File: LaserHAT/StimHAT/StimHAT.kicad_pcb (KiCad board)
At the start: 4 copper layers, 65 x 64.5 mm, 112 parts, among them J1 GPIO, J10 OLED 0.91 (GND VCC SCL SDA), J101 ELECTRODE E1/E2, J102 B4B-PH-K-S(LF)(SN), J103 5V TO DC-DC POD, J5 GT-USB-7010ASV, J6 BNC TRIGGER IN, J7 BNC STIM OUT, Q3 AP30P30Q, Q4 DMMT5401, Q5 AP30P30Q, SW10 MSK12C02, SW6 TS-1088-AR02016, SW7 SKRHADE010, SW9 TS-1088-AR02016, U1 M24C32-WDW6TP, U101 ISO7741FDBQR, U104 TLV76050DBZR, U105 DAC60501ZDGSR, U106 OPA2192IDGKR, U107 CD74HC4053PWR, U108 DG418DY-T1-E3, U109 ISO1640BDR, U110 TLV1702AIDGKR, U4 MCP1700T-3302E/MB, U5 AP2171W, U6 CH340N, U7 MSPM0G1507SRHBR, U8 74LVC2G17GW

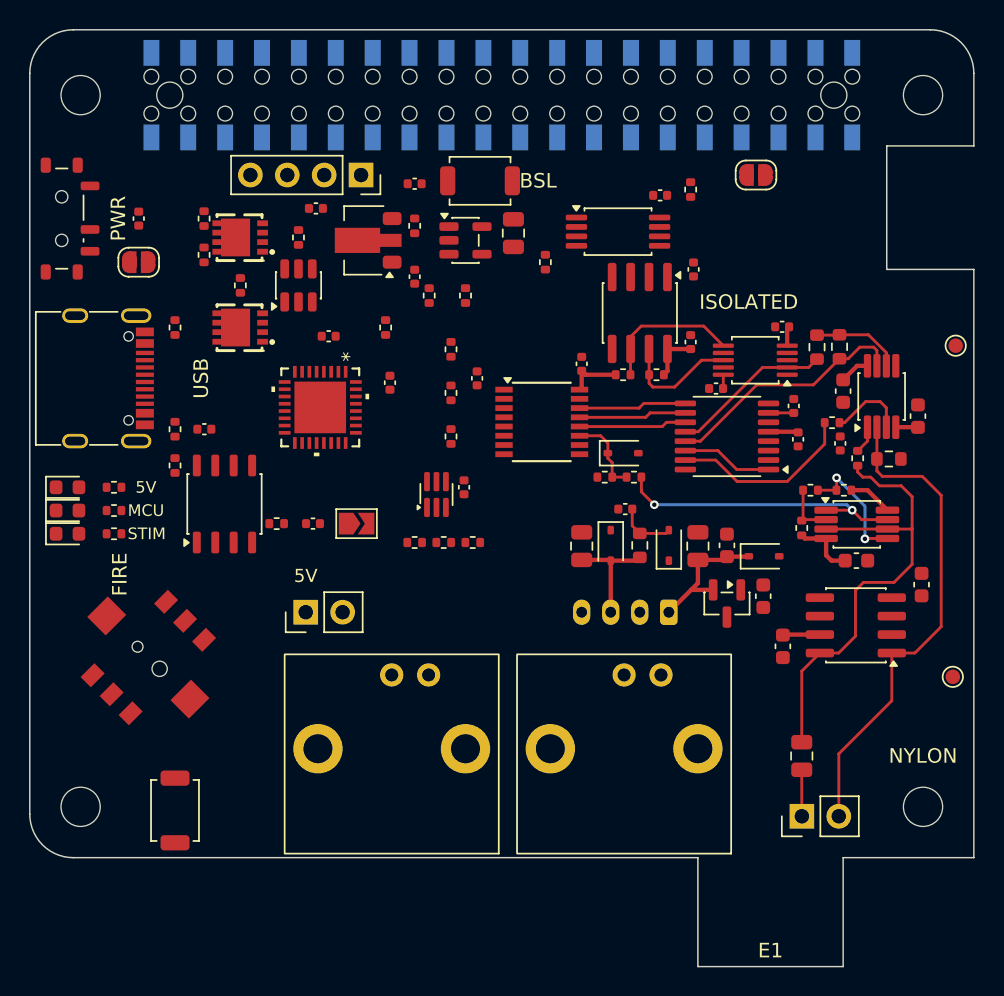
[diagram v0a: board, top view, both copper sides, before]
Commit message: StimHAT: regions/strips/planes reshaped to the user's placement, tab removed, F/B ground pours + In2 power islands, isolated-block power routed (vias to the islands, maze for the negative rails, stitching vias); DRC 0 errors, 123 HAT-side opens
Co-Authored-By: Claude Fable 5.1 <noreply@anthropic.com>
Claude-Session: https://claude.ai/code/session_015kiXLxnPpBaXdXJu2EMvn7
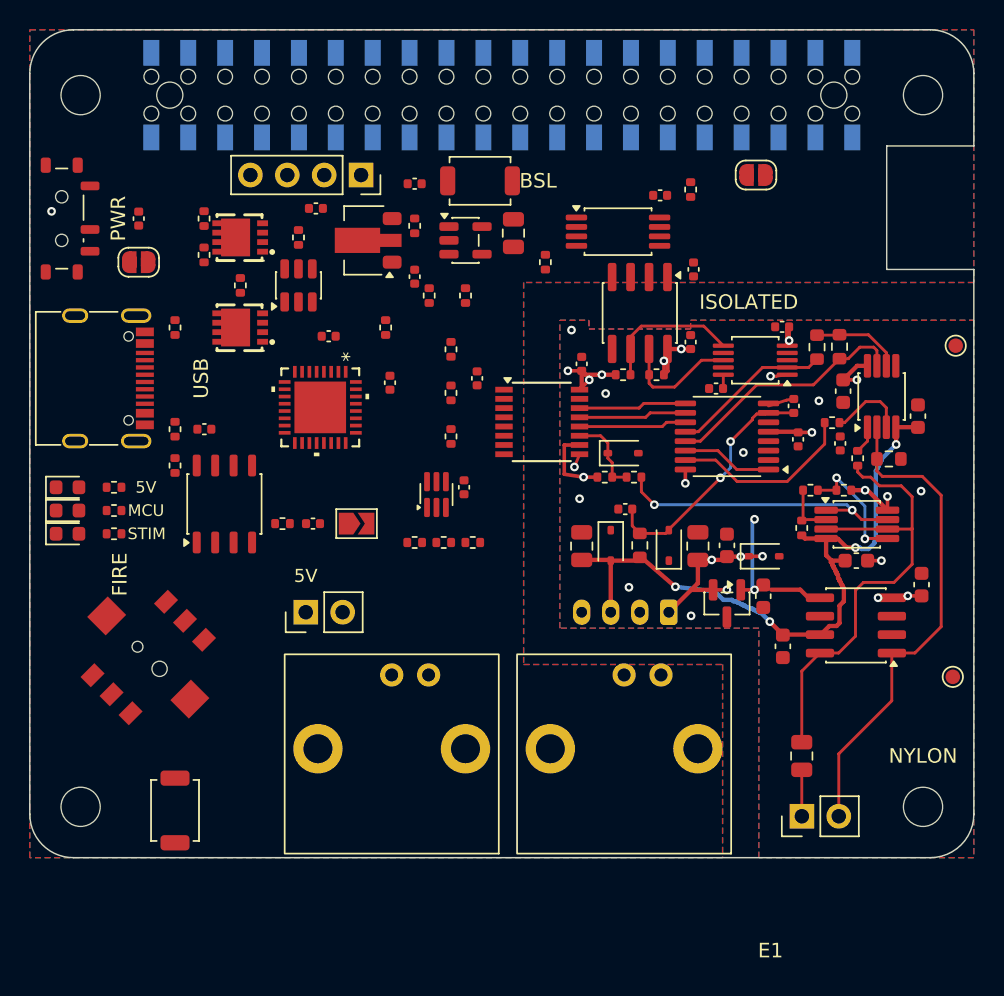
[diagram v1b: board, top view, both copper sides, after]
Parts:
- moved R3 0.40 mm to (17.4, 34.0)
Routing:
- net -V_STIM: track 16.1 -> 46.9 mm, vias 0 -> 4
- net +5V_ISO: track 10.7 -> 34.3 mm, vias 0 -> 12
- net -5V_ISO: track 5.72 -> 17.1 mm, vias 0 -> 2
- net +V_STIM: track 14.7 -> 24.2 mm, vias 0 -> 10
- net GND_ISO: track 0.00 -> 2.74 mm, vias 0 -> 9
- net GND: vias 0 -> 1
- added copper zone on In2.Cu, net +5V
- added copper zone on In2.Cu, net +5V_ISO
- added copper zone on In2.Cu, net +V_STIM
- added copper zone on B.Cu, net GND
- added copper zone on F.Cu, net GND
- added copper zone on B.Cu, net GND_ISO
- added copper zone on F.Cu, net GND_ISO
- added copper zone on In2.Cu, net MSPM0_3V3
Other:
- board size 65 x 64.5 mm -> 65 x 57 mm

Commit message: StimHAT: MCU pin map re-optimised for the placement (isolator lines east on TIMA0 CCP3/CCP1/FAULT0 + ADC0 ch3/ch2, buttons and LED west/south, STIM_IN on TIMG8_CCP0); schematic, board and README updated
Co-Authored-By: Claude Fable 5.1 <noreply@anthropic.com>
Claude-Session: https://claude.ai/code/session_015kiXLxnPpBaXdXJu2EMvn7
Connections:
- U7 pad 10: FAULT_H -> BUTTON4
- U7 pad 11: EN_H -> BUTTON6
- U7 pad 16: CATH_H -> BUTTON2
- U7 pad 17: BUTTON4 -> BUTTON1
- U7 pad 18: BUTTON2 -> BUTTON3
- U7 pad 20: BUTTON3 -> BUTTON5
- U7 pad 21: SDA_H -> MCU_STIM_OUT
- U7 pad 25: BUTTON1 -> MCU_STIM_IN
- U7 pad 26: SCL_H -> CATH_H
- U7 pad 27: BUTTON5 -> EN_H
- U7 pad 28: LED_MCU -> SDA_H
- U7 pad 29: MCU_STIM_OUT -> SCL_H
- U7 pad 30: MCU_STIM_IN -> FAULT_H
- U7 pad 7: BUTTON6 -> unconnected-(U7-PA3-Pad7)
- U7 pad 9: unconnected-(U7-PA5-Pad9) -> LED_MCU
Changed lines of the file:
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@@
 	(net 103 "unconnected-(U5-~{FLG}-Pad3)")
 	(net 104 "unconnected-(U7-PA4-Pad8)")
-	(net 105 "unconnected-(U7-PA5-Pad9)")
-	(net 106 "/VREFIO")
-	(net 107 "OA_IN")
-	(net 108 "OA_OUT")
-	(net 109 "U5B_IN")
+	(net 105 "/VREFIO")
+	(net 106 "OA_IN")
+	(net 107 "OA_OUT")
+	(net 108 "U5B_IN")
+	(net 109 "unconnected-(U7-PA3-Pad7)")
 	(footprint "Capacitor_SMD:C_0402_1005Metric"
 		(layer "F.Cu")
@@
 			(layers "F.Cu" "F.Mask" "F.Paste")
 			(roundrect_rratio 0.25)
-			(net 109 "U5B_IN")
+			(net 108 "U5B_IN")
 			(pintype "passive")
 		)
@@
 			(layers "F.Cu" "F.Mask" "F.Paste")
 			(roundrect_rratio 0.25)
-			(net 106 "/VREFIO")
+			(net 105 "/VREFIO")
 			(pintype "passive")
 		)
@@
 			(layers "F.Cu" "F.Mask" "F.Paste")
 			(roundrect_rratio 0.25)
-			(net 107 "OA_IN")
+			(net 106 "OA_IN")
 			(pintype "passive")
 		)
@@
 			(layers "F.Cu" "F.Mask" "F.Paste")
 			(roundrect_rratio 0.25)
-			(net 107 "OA_IN")
+			(net 106 "OA_IN")
 			(pintype "passive")
 		)
@@
 			(layers "F.Cu" "F.Mask" "F.Paste")
 			(roundrect_rratio 0.25)
-			(net 108 "OA_OUT")
+			(net 107 "OA_OUT")
 			(pintype "passive")
 		)
@@
 			(layers "F.Cu" "F.Mask" "F.Paste")
 			(roundrect_rratio 0.25)
-			(net 108 "OA_OUT")
+			(net 107 "OA_OUT")
 			(pintype "output")
 		)
@@
 			(layers "F.Cu" "F.Mask" "F.Paste")
 			(roundrect_rratio 0.25)
-			(net 107 "OA_IN")
+			(net 106 "OA_IN")
 			(pinfunction "+")
 			(pintype "input")
@@
 			(layers "F.Cu" "F.Mask" "F.Paste")
 			(roundrect_rratio 0.25)
-			(net 109 "U5B_IN")
+			(net 108 "U5B_IN")
 			(pinfunction "-")
 			(pintype "input")
@@
 			(size 0.254 0.8128)
 			(layers "F.Cu" "F.Mask" "F.Paste")
-			(net 23 "BUTTON6")
+			(net 109 "unconnected-(U7-PA3-Pad7)")
 			(pinfunction "PA3")
 			(pintype "bidirectional")
@@
 			(size 0.254 0.8128)
 			(layers "F.Cu" "F.Mask" "F.Paste")
-			(net 105 "unconnected-(U7-PA5-Pad9)")
+			(net 40 "LED_MCU")
 			(pinfunction "PA5")
 			(pintype "bidirectional+no_connect")
@@
 			(size 0.254 0.8128)
 			(layers "F.Cu" "F.Mask" "F.Paste")
-			(net 30 "FAULT_H")
+			(net 21 "BUTTON4")
 			(pinfunction "PA6")
 			(pintype "bidirectional")
@@
 			(size 0.254 0.8128)
 			(layers "F.Cu" "F.Mask" "F.Paste")
-			(net 29 "EN_H")
+			(net 23 "BUTTON6")
 			(pinfunction "PA7")
 			(pintype "bidirectional")
@@
 			(size 0.254 0.8128)
 			(layers "F.Cu" "F.Mask" "F.Paste")
-			(net 25 "CATH_H")
+			(net 19 "BUTTON2")
 			(pinfunction "PA12")
 			(pintype "bidirectional")
@@
 			(size 0.254 0.8128)
 			(layers "F.Cu" "F.Mask" "F.Paste")
-			(net 21 "BUTTON4")
+			(net 18 "BUTTON1")
 			(pinfunction "PA13")
 			(pintype "bidirectional")
@@
 			(size 0.254 0.8128)
 			(layers "F.Cu" "F.Mask" "F.Paste")
-			(net 19 "BUTTON2")
+			(net 20 "BUTTON3")
 			(pinfunction "PA14")
 			(pintype "bidirectional")
@@
 			(size 0.254 0.8128)
 			(layers "F.Cu" "F.Mask" "F.Paste")
-			(net 20 "BUTTON3")
+			(net 22 "BUTTON5")
 			(pinfunction "PA16")
 			(pintype "bidirectional")
@@
 			(size 0.254 0.8128)
 			(layers "F.Cu" "F.Mask" "F.Paste")
-			(net 67 "SDA_H")
+			(net 43 "MCU_STIM_OUT")
 			(pinfunction "PA17")
 			(pintype "bidirectional")
@@
 			(size 0.254 0.8128)
 			(layers "F.Cu" "F.Mask" "F.Paste")
-			(net 18 "BUTTON1")
+			(net 42 "MCU_STIM_IN")
 			(pinfunction "PA21")
 			(pintype "bidirectional")
@@
 			(size 0.254 0.8128)
 			(layers "F.Cu" "F.Mask" "F.Paste")
-			(net 65 "SCL_H")
+			(net 25 "CATH_H")
 			(pinfunction "PA22")
 			(pintype "bidirectional")
@@
 			(size 0.254 0.8128)
 			(layers "F.Cu" "F.Mask" "F.Paste")
-			(net 22 "BUTTON5")
+			(net 29 "EN_H")
 			(pinfunction "PA23")
 			(pintype "bidirectional")
@@
 			(size 0.254 0.8128)
 			(layers "F.Cu" "F.Mask" "F.Paste")
-			(net 40 "LED_MCU")
+			(net 67 "SDA_H")
 			(pinfunction "PA24")
 			(pintype "bidirectional")
@@
 			(size 0.254 0.8128)
 			(layers "F.Cu" "F.Mask" "F.Paste")
-			(net 43 "MCU_STIM_OUT")
+			(net 65 "SCL_H")
 			(pinfunction "PA25")
 			(pintype "bidirectional")
@@
 			(size 0.254 0.8128)
 			(layers "F.Cu" "F.Mask" "F.Paste")
-			(net 42 "MCU_STIM_IN")
+			(net 30 "FAULT_H")
 			(pinfunction "PA26")
 			(pintype "bidirectional")
@@
 			(layers "F.Cu" "F.Mask" "F.Paste")
 			(roundrect_rratio 0.25)
-			(net 106 "/VREFIO")
+			(net 105 "/VREFIO")
 			(pinfunction "VREFIO")
 			(pintype "passive")
@@
 			(layers "F.Cu" "F.Mask" "F.Paste")
 			(roundrect_rratio 0.25)
-			(net 109 "U5B_IN")
+			(net 108 "U5B_IN")
 			(pintype "passive")
 		)
@@
 		(width 0.2)
 		(layer "F.Cu")
-		(net 106)
+		(net 105)
 	)
 	(segment
@@
 		(width 0.2)
 		(layer "F.Cu")
-		(net 106)
+		(net 105)
 	)
 	(segment
@@
 		(width 0.2)
 		(layer "F.Cu")
-		(net 107)
+		(net 106)
 	)
 	(segment
@@
 		(width 0.2)
 		(layer "F.Cu")
-		(net 107)
+		(net 106)
 	)
 	(segment
@@
 		(width 0.2)
 		(layer "F.Cu")
-		(net 107)
+		(net 106)
 	)
 	(segment
@@
 		(width 0.2)
 		(layer "F.Cu")
-		(net 107)
+		(net 106)
 	)
 	(segment
@@
 		(width 0.2)
 		(layer "F.Cu")
-		(net 107)
+		(net 106)
 	)
 	(segment
@@
 		(width 0.2)
 		(layer "F.Cu")
-		(net 108)
+		(net 107)
 	)
 	(segment
@@
 		(width 0.2)
 		(layer "F.Cu")
-		(net 108)
+		(net 107)
 	)
 	(segment
@@
 		(width 0.2)
 		(layer "F.Cu")
-		(net 108)
+		(net 107)
 	)
 	(segment
@@
 		(width 0.2)
 		(layer "F.Cu")
-		(net 109)
+		(net 108)
 	)
 	(segment
@@
 		(width 0.2)
 		(layer "F.Cu")
-		(net 109)
+		(net 108)
 	)
 	(segment
@@
 		(width 0.2)
 		(layer "F.Cu")
-		(net 109)
+		(net 108)
 	)
 	(segment
@@
 		(width 0.2)
 		(layer "F.Cu")
-		(net 109)
+		(net 108)
 	)
 	(segment
@@
 		(width 0.2)
 		(layer "F.Cu")
-		(net 109)
+		(net 108)
 	)
 	(zone

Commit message: StimHAT: In2 is a routing layer (power islands dropped), isolated rails joined on In2 as tracks; OLED module drawn lying flat along the header
Co-Authored-By: Claude Fable 5.1 <noreply@anthropic.com>
Claude-Session: https://claude.ai/code/session_015kiXLxnPpBaXdXJu2EMvn7
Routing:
- net +5V_ISO: track 34.3 -> 85.0 mm
- net +V_STIM: track 24.2 -> 62.5 mm
- removed copper zone on In2.Cu, net +5V
- removed copper zone on In2.Cu, net +5V_ISO
- removed copper zone on In2.Cu, net +V_STIM
- removed copper zone on In2.Cu, net MSPM0_3V3
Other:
- board text added: "0.91in OLED module lying flat on J10 (right-angle pins), 8.5 mm up, pins = top edge"
- board text removed: "0.91in OLED module standing in J10 (38 x 12, 8.5 mm up)"

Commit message: StimHAT: drop the redundant In2 +5V_ISO detour that crossed the +V_STIM link (the two vias are joined on the back); DRC 0 errors
Co-Authored-By: Claude Fable 5.1 <noreply@anthropic.com>
Claude-Session: https://claude.ai/code/session_015kiXLxnPpBaXdXJu2EMvn7
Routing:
- net +5V_ISO: track 85.0 -> 76.2 mm
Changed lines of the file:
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@@
-	)
-	(segment
-		(start 51.9 38.5625)
-		(end 49.9 38.5625)
-		(width 0.3)
-		(layer "In2.Cu")
-		(net 4)
 	)
 	(segment
@@
 	)
 	(segment
-		(start 49.9 33.7)
-		(end 51.9 33.7)
-		(width 0.3)
-		(layer "In2.Cu")
-		(net 4)
-	)
-	(segment
 		(start 38.129999 30.8)
 		(end 38.521751 30.8)
@@
 		(width 0.3)
 		(layer "In2.Cu")
-		(net 4)
-	)
-	(segment
-		(start 51.9 33.7)
-		(end 51.9 38.5625)
-		(width 0.3)
-		(layer "In2.Cu")

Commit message: StimHAT: OLED module drawn both ways (standing with straight pins, flat with right-angle pins) on J10's vertical socket
Co-Authored-By: Claude Fable 5.1 <noreply@anthropic.com>
Claude-Session: https://claude.ai/code/session_015kiXLxnPpBaXdXJu2EMvn7
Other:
- board text added: "0.91in OLED module on J10 (vertical socket): straight pins -> standing along the header (strip), right-angle pins -> lying flat (rect)"
- board text removed: "0.91in OLED module lying flat on J10 (right-angle pins), 8.5 mm up, pins = top edge"
